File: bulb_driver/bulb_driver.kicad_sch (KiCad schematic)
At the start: 10 parts, among them J1 Conn_01x02, U1 LM3410DGN, U2 ATtiny13-20S, U3 AP9101CK6

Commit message: Update schematic
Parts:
- removed U2: ATtiny13-20S, Package_SO:SOIC-8W_5.3x5.3mm_P1.27mm, symbol MCU_Microchip_ATtiny:ATtiny13-20S
- added C3, C4: 10u, symbol Device:C
- added D2: 23V, symbol Device:D_Zener
- added R2: 39R, symbol Device:R
- added U2: ATtiny1614-SS, Package_SO:SOIC-14_3.9x8.7mm_P1.27mm, symbol MCU_Microchip_ATtiny:ATtiny1614-SS
- C1: value C -> 10u
- D1: value D_Schottky -> SS34
- J1: value Conn_01x02 -> LED_OUT
- L1: value L -> 150u
- R1: value R -> 1R
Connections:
- net GND: now also C3.2, C4.2
- net VCC: now also C3.1
- net at J1.2 (Pin_2), R1.1: now also R2.2; no longer U1.5 (FB)
- net at C2.1, D1.1 (K), J1.1 (Pin_1): now also C4.1, D2.1 (K)
- new net: D2.2 (A), R2.1, U1.5 (FB)
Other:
- note added: "dV = 0,025×(21,6×0,89/(2×525000×2×0,00001)) Dmax = (21,6 - 0,8*3,2)/21,6 dL = 5/0,000360×0,89×(1/525000) Rout = 190/200 = 0,95 ~ 1R"
- note added: "strona 13 Iout max to 200mA przy 21,6V Imax to około 1,4A dIl to około 25mA dV to około 22mV @10uF wyj zzakładam Dmax = 0,89 eff min 80%"
- moved on the sheet: C1, C2, D1, J1, L1, R1, U1, U3

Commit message: Project update
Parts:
- removed BT1: 18650 Battery holder, symbol Device:Battery_Cell
- removed U2: ATtiny1614-SS, Package_SO:SOIC-14_3.9x8.7mm_P1.27mm, symbol MCU_Microchip_ATtiny:ATtiny1614-SS
- removed U3: AP9101CK6, Package_TO_SOT_SMD:SOT-23-6, symbol Battery_Management:AP9101CK6
- added H1, H2, H3, H4: M3, MountingHole:MountingHole_3.2mm_M3_Pad_Via, symbol Mechanical:MountingHole_Pad
- added J1: PWR_IN, Connector_Wire:SolderWire-1sqmm_1x02_P7.8mm_D1.4mm_OD3.9mm, symbol Connector_Generic:Conn_01x02
- added J2: DIMM, Connector_PinHeader_2.54mm:PinHeader_1x02_P2.54mm_Vertical, symbol Connector_Generic:Conn_01x02
- added R3: 10k, Resistor_SMD:R_0805_2012Metric, symbol Device:R
- added R4: 1R, Resistor_SMD:R_0805_2012Metric, symbol Device:R
- C1, C2, C3, C4: footprint (none) -> Capacitor_SMD:C_1210_3225Metric
- D1: footprint (none) -> Diode_SMD:D_SMC
- D2: footprint (none) -> Diode_SMD:D_SOD-123
- J3: renamed from J1; footprint (none) -> Connector_Wire:SolderWire-1sqmm_1x02_P7.8mm_D1.4mm_OD3.9mm
- L1: footprint (none) -> Inductor_SMD:L_Bourns_SRR1210A
- R1, R2: footprint (none) -> Resistor_SMD:R_0805_2012Metric
- U1: footprint Package_SO:TI_SO-PowerPAD-8_ThermalVias -> projectfb:HVSSOP-8-1EP_3x3mm_P0.65mm_EP1.57x1.89mm
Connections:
- net GND: now also H1.1, H2.1, H3.1, H4.1, J1.1 (Pin_1), J2.1 (Pin_1), R4.2
- net PWM: now also J2.2 (Pin_2), R3.2
- net VCC: now also J1.2 (Pin_2), R3.1
- net FEEDBACK: now reaches D2.2 (A), R2.1, U1.5 (FB)
- net LED-: now reaches J3.2 (Pin_2), R1.1, R2.2
- net LED-: now also R4.1
- net LED+: now reaches C2.1, C4.1, D1.1 (K), D2.1 (K), J3.1 (Pin_1)
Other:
- note removed: "dV = 0,025×(21,6×0,89/(2×525000×2×0,00001)) Dmax = (21,6 - 0,8*3,2)/21,6 dL = 5/0,000360×0,89×(1/525000) Rout = 190/200 = 0,95 ~ 1R"
- note removed: "strona 13 Iout max to 200mA przy 21,6V Imax to około 1,4A dIl to około 25mA dV to około 22mV @10uF wyj zzakładam Dmax = 0,89 eff min 80%"
- moved on the sheet: C1, C2, C3, C4, D1, D2, J3, L1, R1, R2, U1

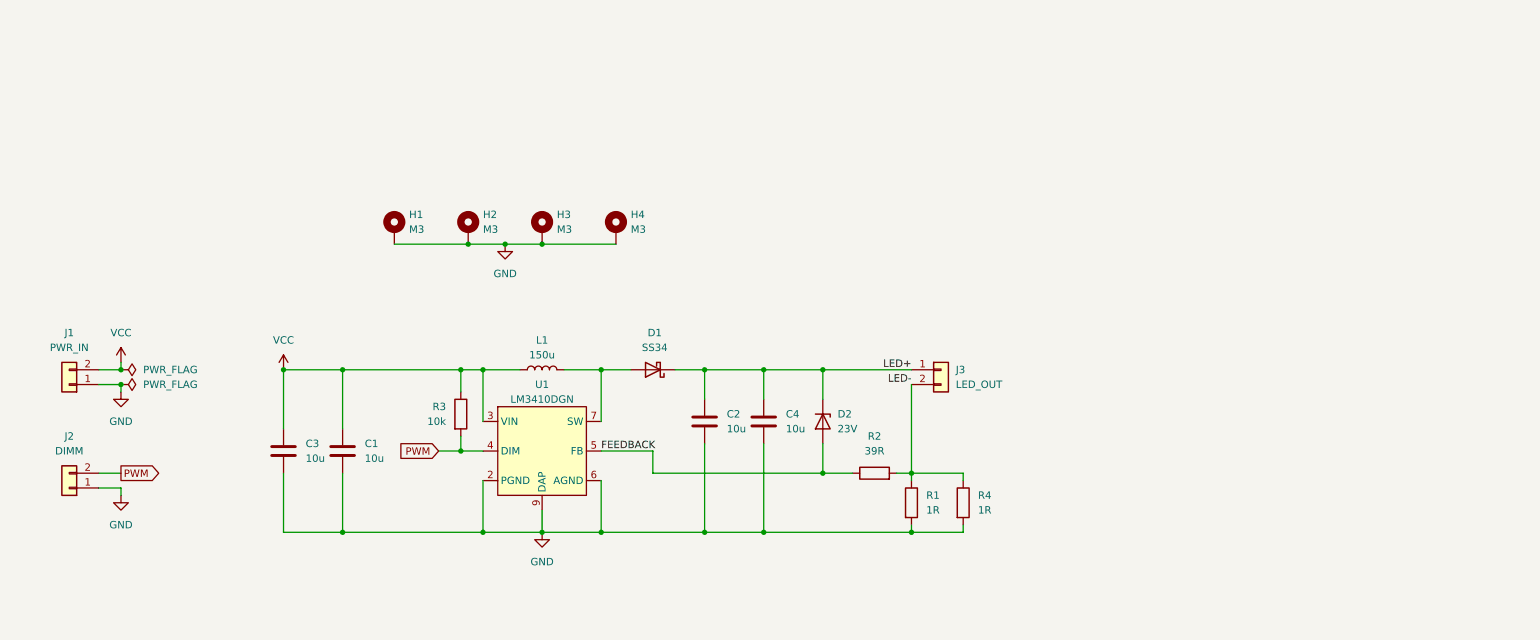
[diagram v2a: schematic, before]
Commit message: Create target design schematic structure
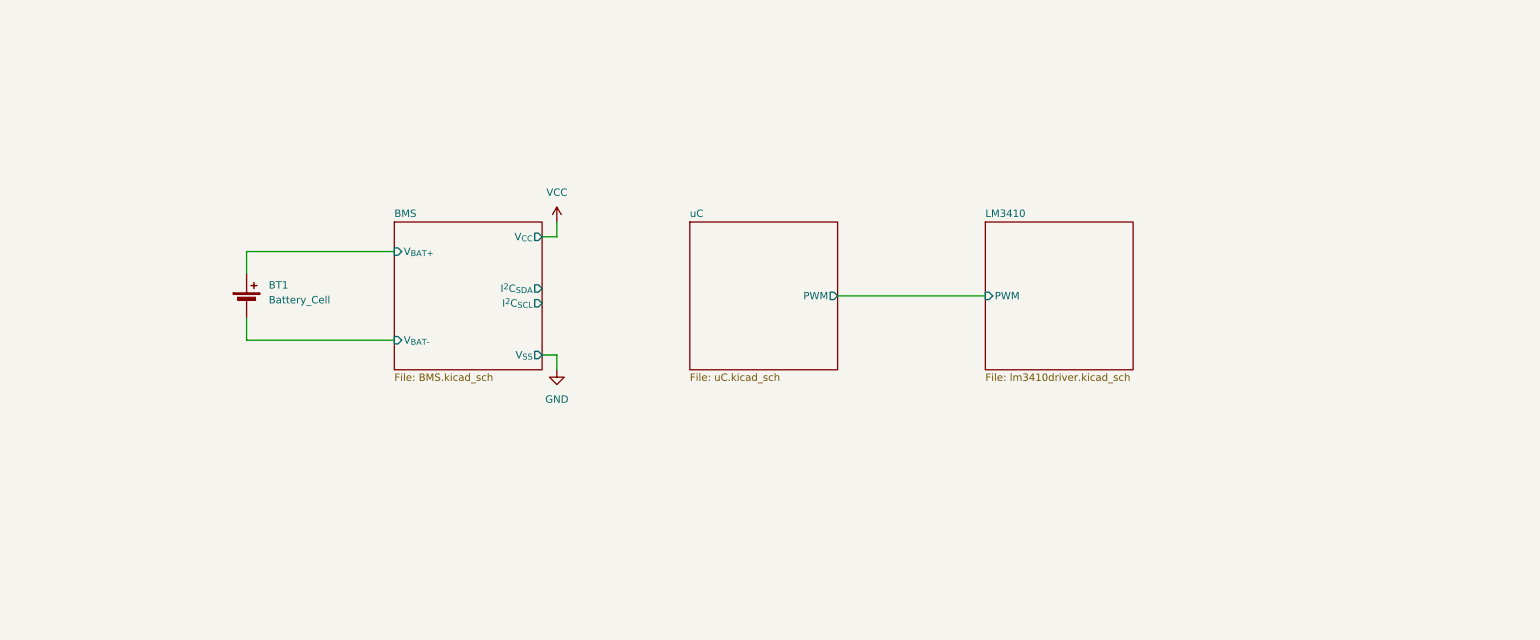
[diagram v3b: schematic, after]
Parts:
- removed C1, C2, C3, C4: 10u, Capacitor_SMD:C_1210_3225Metric, symbol Device:C
- removed D1: SS34, Diode_SMD:D_SMC, symbol Device:D_Schottky
- removed D2: 23V, Diode_SMD:D_SOD-123, symbol Device:D_Zener
- removed H1, H2, H3, H4: M3, MountingHole:MountingHole_3.2mm_M3_Pad_Via, symbol Mechanical:MountingHole_Pad
- removed J1: PWR_IN, Connector_Wire:SolderWire-1sqmm_1x02_P7.8mm_D1.4mm_OD3.9mm, symbol Connector_Generic:Conn_01x02
- removed J2: DIMM, Connector_PinHeader_2.54mm:PinHeader_1x02_P2.54mm_Vertical, symbol Connector_Generic:Conn_01x02
- removed J3: LED_OUT, Connector_Wire:SolderWire-1sqmm_1x02_P7.8mm_D1.4mm_OD3.9mm, symbol Connector_Generic:Conn_01x02
- removed L1: 150u, Inductor_SMD:L_Bourns_SRR1210A, symbol Device:L
- removed R1, R4: 1R, Resistor_SMD:R_0805_2012Metric, symbol Device:R
- removed R2: 39R, Resistor_SMD:R_0805_2012Metric, symbol Device:R
- removed R3: 10k, Resistor_SMD:R_0805_2012Metric, symbol Device:R
- removed U1: LM3410DGN, projectfb:HVSSOP-8-1EP_3x3mm_P0.65mm_EP1.57x1.89mm, symbol project_lib:LM3410DGN
- added BT1: Battery_Cell, symbol Device:Battery_Cell
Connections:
- new net BMS/V_{BAT+}: BT1.1 (+)
- new net BMS/V_{BAT-}: BT1.2 (-)
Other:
- added sheet BMS (BMS.kicad_sch)
- added sheet LM3410 (lm3410driver.kicad_sch)
- added sheet uC (uC.kicad_sch)

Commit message: Project update
Add USB and Touch sheets

Make initial schematic for uC block
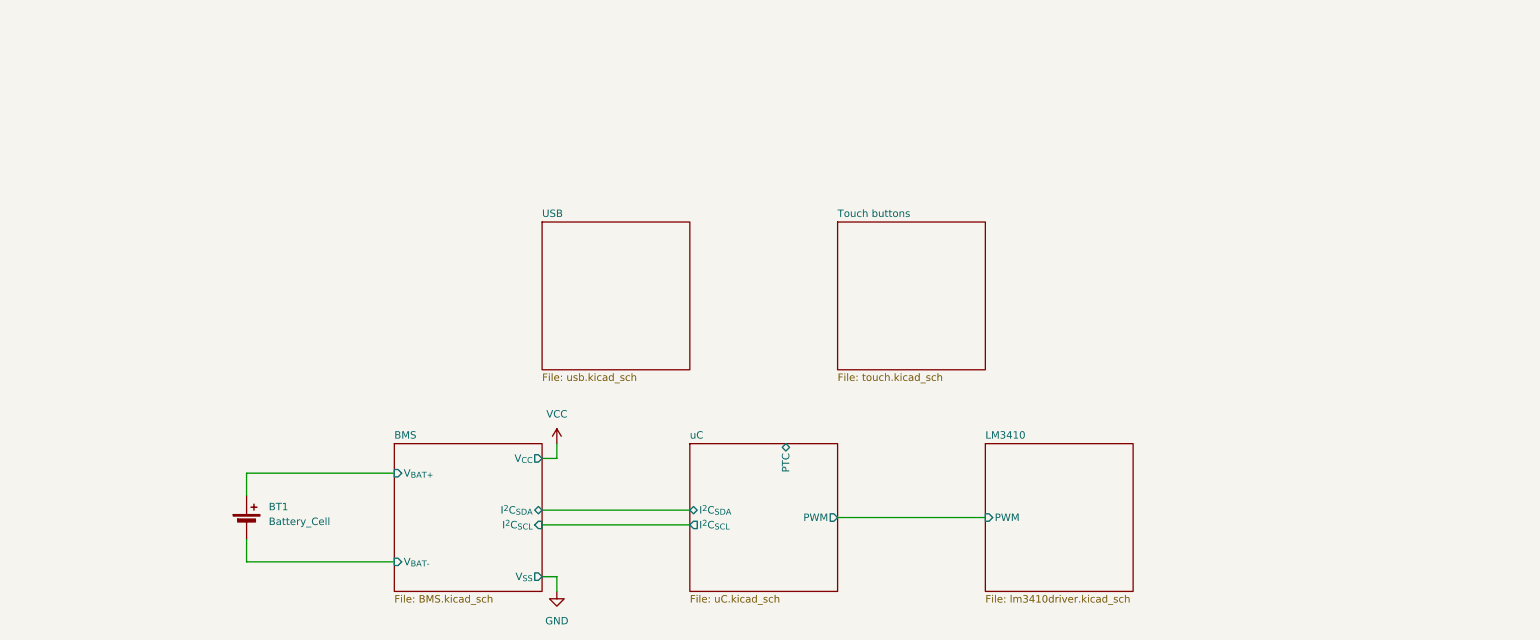
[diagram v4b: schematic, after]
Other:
- added sheet Touch buttons (touch.kicad_sch)
- added sheet USB (usb.kicad_sch)
- sheet uC ports: added I^{2}C_{SCL}, I^{2}C_{SDA}, PTC; removed none
- moved on the sheet: BT1

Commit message: Update KiCad project files
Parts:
- removed BT1: Battery_Cell, symbol Device:Battery_Cell
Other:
- sheet BMS renamed BMS and Battery
- sheet BMS and Battery ports: added none; removed I^{2}C_{SCL}, I^{2}C_{SDA}, V_{BAT+}, V_{BAT-}, V_{CC}, V_{SS}

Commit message: Update schematics
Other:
- sheet BMS and Battery: file BMS.kicad_sch -> battery.kicad_sch
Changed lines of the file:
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@@
 			)
 		)
-		(property "Sheetfile" "BMS.kicad_sch"
+		(property "Sheetfile" "battery.kicad_sch"
 			(at 88.9 114.8846 0)
 			(effects
@@
 	)
 	(sheet
-		(at 165.1 50.8)
+		(at 139.7 50.8)
 		(size 25.4 25.4)
 		(fields_autoplaced yes)
@@
 		)
 		(property "Sheetname" "Touch buttons"
-			(at 165.1 50.0884 0)
+			(at 139.7 50.0884 0)
 			(effects
 				(font
@@
 		)
 		(property "Sheetfile" "touch.kicad_sch"
-			(at 165.1 76.7846 0)
+			(at 139.7 76.7846 0)
 			(effects
 				(font
